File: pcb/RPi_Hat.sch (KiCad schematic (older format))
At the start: 0 parts

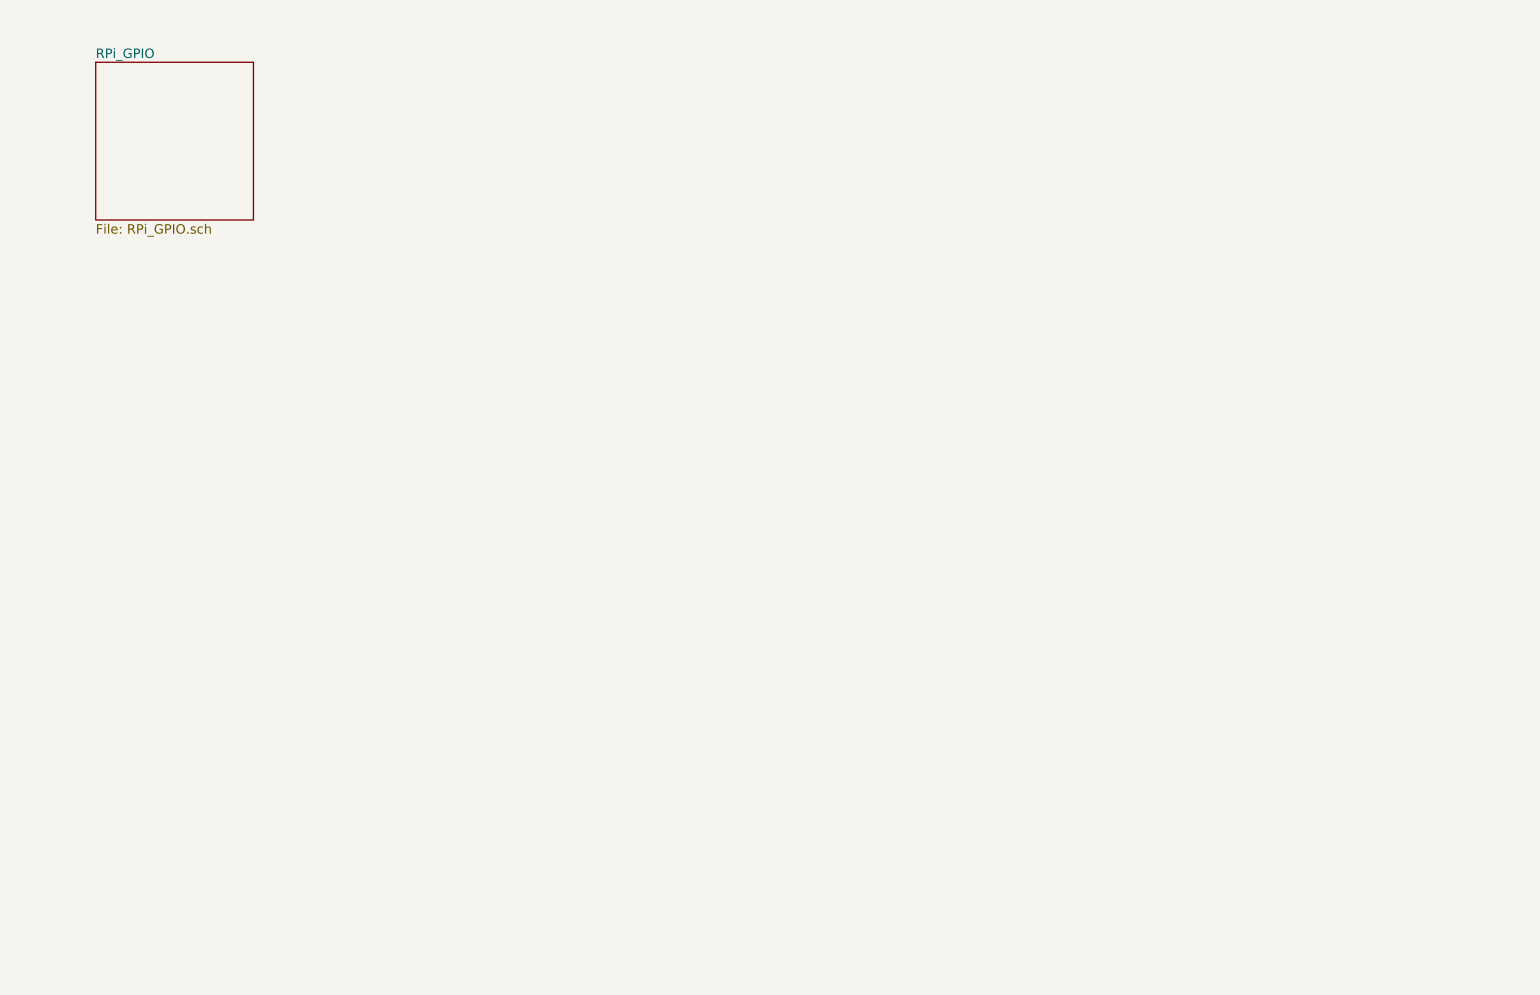
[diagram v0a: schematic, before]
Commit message: Schematic updates
Don't use a relay, use a level shifter so the pin can be used as either
an input or an output.
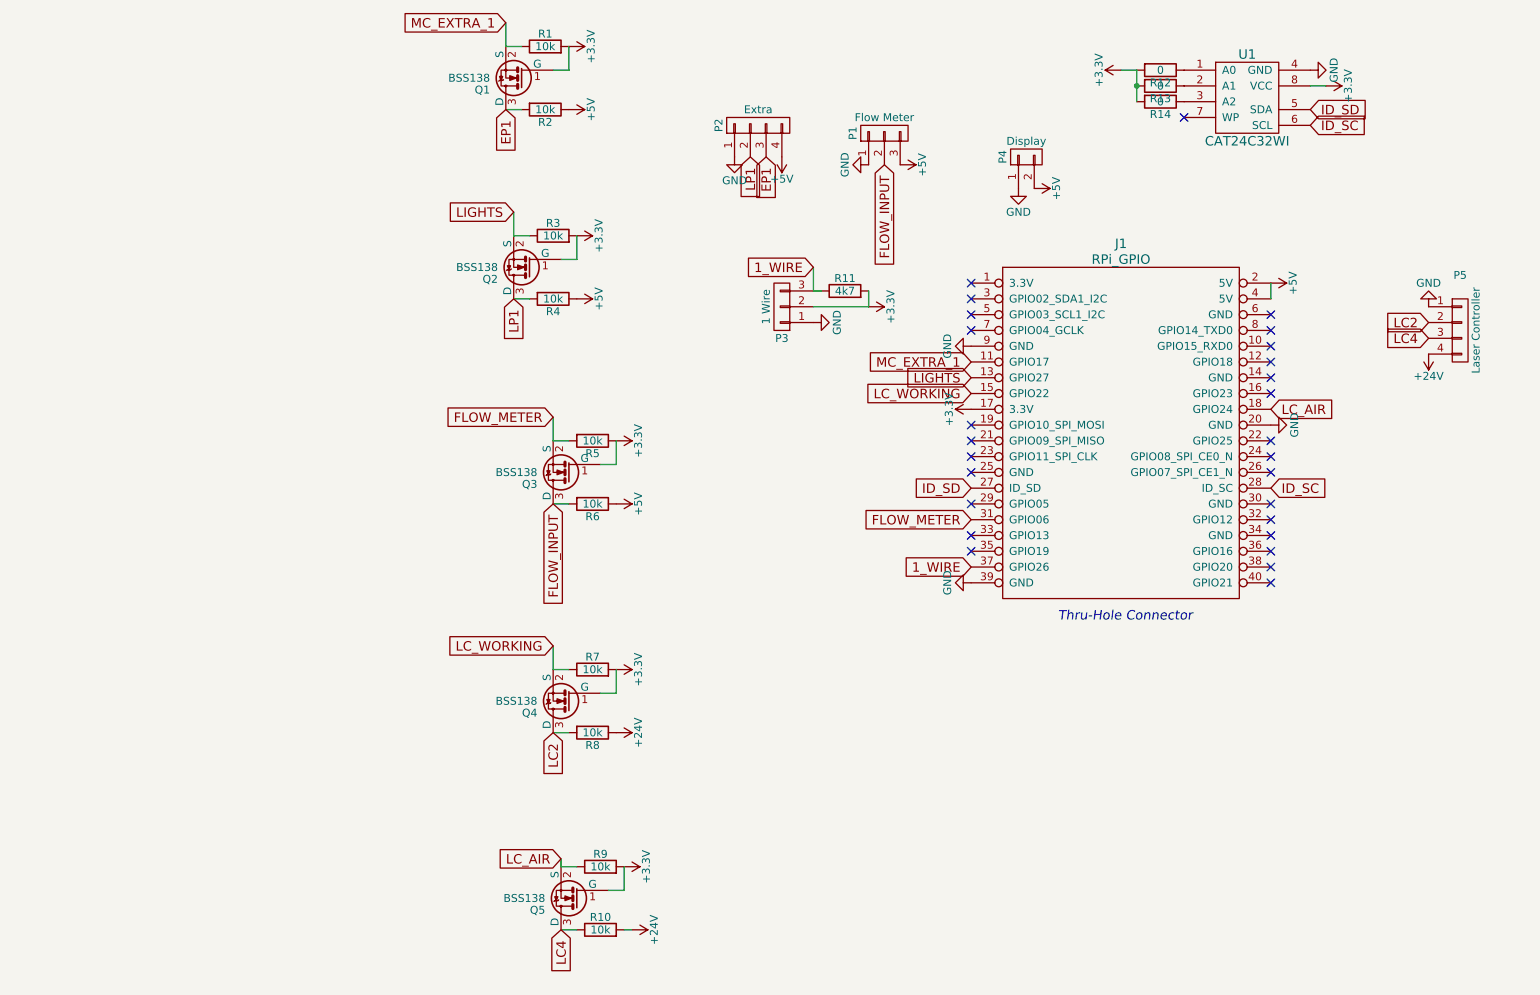
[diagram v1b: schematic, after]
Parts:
- added J1: RPi_GPIO, RPi_Hat:Pin_Header_Straight_2x20, symbol RPi_GPIO
- added P1: Flow Meter, Terminal_Blocks:TerminalBlock_Pheonix_MPT-2.54mm_3pol, symbol CONN_01X03
- added P2: Extra, Terminal_Blocks:TerminalBlock_Pheonix_MPT-2.54mm_5pol, symbol CONN_01X04
- added P3: 1 Wire, Terminal_Blocks:TerminalBlock_Pheonix_MPT-2.54mm_3pol, symbol CONN_01X03
- added P4: Display, Terminal_Blocks:TerminalBlock_Pheonix_MPT-2.54mm_2pol, symbol CONN_01X02
- added P5: Laser Controller, Terminal_Blocks:TerminalBlock_Pheonix_MPT-2.54mm_4pol, symbol CONN_01X04
- added Q1, Q2, Q3, Q4, Q5: BSS138, TO_SOT_Packages_SMD:SOT-23, symbol BSS138
- added R1, R10, R2, R3, R4, R5, R6, R7, R8, R9: 10k, Resistors_SMD:R_1206_HandSoldering, symbol R
- added R11: 4k7, Resistors_SMD:R_1206_HandSoldering, symbol R
- added R12, R13, R14: 0, Resistors_SMD:R_0402, symbol R
- added U1: CAT24C32WI, SMD_Packages:SOIC-8-N, symbol CAT24C32WI
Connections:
- new net: R12.1, U1.1 (A0)
- new net: R13.1, U1.2 (A1)
- new net: R14.1, U1.3 (A2)
- new net +24V: P5.4 (P4), R10.2, R8.1
- new net +3V3: J1.17 (3.3V), P3.2 (P2), Q1.1 (G), Q2.1 (G), Q3.1 (G), Q4.1 (G), Q5.1 (G), R1.2, R11.2, R12.2, R13.2, R14.2, R3.2, R5.1, R7.2, R9.2, U1.8 (VCC)
- new net +5V: J1.2 (5V), J1.4 (5V), P1.3 (P3), P2.4 (P4), P4.2 (P2), R2.1, R4.1, R6.1
- new net 1_WIRE: J1.37 (GPIO26), P3.3 (P3), R11.1
- new net EP1: P2.3 (P3), Q1.3 (D), R2.2
- new net FLOW_INPUT: P1.2 (P2), Q3.3 (D), R6.2
- new net FLOW_METER: J1.31 (GPIO06), Q3.2 (S), R5.2
- new net GND: J1.20 (GND), J1.39 (GND), J1.9 (GND), P1.1 (P1), P2.1 (P1), P3.1 (P1), P4.1 (P1), P5.1 (P1), U1.4 (GND)
- new net ID_SC: J1.28 (ID_SC), U1.6 (SCL)
- new net ID_SD: J1.27 (ID_SD), U1.5 (SDA)
- new net LC2: P5.2 (P2), Q4.3 (D), R8.2
- new net LC4: P5.3 (P3), Q5.3 (D), R10.1
- new net LC_AIR: J1.18 (GPIO24), Q5.2 (S), R9.1
- new net LC_WORKING: J1.15 (GPIO22), Q4.2 (S), R7.1
- new net LIGHTS: J1.13 (GPIO27), Q2.2 (S), R3.1
- new net LP1: P2.2 (P2), Q2.3 (D), R4.2
- new net MC_EXTRA_1: J1.11 (GPIO17), Q1.2 (S), R1.1
- no-connect marks 0 -> 27
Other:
- note added: "Thru-Hole Connector"

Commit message: Add outputs
for the chiller, exhaust, air
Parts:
- added P6: Laser Controller, Terminal_Blocks:TerminalBlock_Pheonix_MPT-2.54mm_4pol, symbol CONN_01X04
- added Q6, Q7, Q8: PZT2222A, TO_SOT_Packages_SMD:SOT-23, symbol PZT2222A
- added R15, R16, R17, R18, R19, R20: 4K7, Resistors_SMD:R_1206_HandSoldering, symbol R
- P2: footprint Terminal_Blocks:TerminalBlock_Pheonix_MPT-2.54mm_5pol -> Terminal_Blocks:TerminalBlock_Pheonix_MPT-2.54mm_4pol
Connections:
- net +5V: now also R18.1, R19.1, R20.1
- net FLOW_METER: now also J1.35 (GPIO19); no longer J1.31 (GPIO06)
- net GND: now also P6.1 (P1), Q6.3 (E), Q7.3 (E), Q8.3 (E)
- net OUT_EXHAUST: now reaches J1.29 (GPIO05)
- net OUT_EXHAUST: now also R15.2
- net OUT_AIR: now reaches J1.33 (GPIO13)
- net OUT_AIR: now also R17.2
- new net: Q7.1 (B), R16.1, R19.2
- new net: Q6.1 (B), R15.1, R18.2
- new net: Q8.1 (B), R17.1, R20.2
- new net HEADER_AIR: P6.2 (P2), Q8.2 (C)
- new net HEADER_CHILLER: P6.3 (P3), Q7.2 (C)
- new net HEADER_EXHAUST: P6.4 (P4), Q6.2 (C)
- new net OUT_CHILLER: J1.31 (GPIO06), R16.2
- no-connect marks 27 -> 24
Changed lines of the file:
@@
 	0    1    1    0
 $EndComp
-Text GLabel 6950 4300 0    60   Input ~ 0
+Text GLabel 6950 4500 0    60   Input ~ 0
 FLOW_METER
 $Comp
@@
 F 0 "P2" H 5600 2050 50  0000 C CNN
 F 1 "Extra" V 5700 1800 50  0000 C CNN
-F 2 "Terminal_Blocks:TerminalBlock_Pheonix_MPT-2.54mm_5pol" V 5800 1750 50  0001 C CNN
+F 2 "Terminal_Blocks:TerminalBlock_Pheonix_MPT-2.54mm_4pol" V 5800 1750 50  0001 C CNN
 F 3 "" H 5600 1800 50  0000 C CNN
 	1    5600 1800
@@
 NoConn ~ 6950 3800
 NoConn ~ 6950 3900
-NoConn ~ 6950 4200
-NoConn ~ 6950 4400
-NoConn ~ 6950 4500
 NoConn ~ 8300 1750
 NoConn ~ 6950 4000
@@
 Text GLabel 4300 4200 3    60   Input ~ 0
 FLOW_INPUT
+Text GLabel 6950 4400 0    60   Input ~ 0
+OUT_AIR
+Text GLabel 6950 4300 0    60   Input ~ 0
+OUT_CHILLER
+Text GLabel 6950 4200 0    60   Input ~ 0
+OUT_EXHAUST
+$Comp
+L PZT2222A Q7
+U 1 1 5705A6E9
+P 2200 5600
+F 0 "Q7" H 2400 5675 50  0000 L CNN
+F 1 "PZT2222A" H 2400 5600 50  0000 L CNN
+F 2 "TO_SOT_Packages_SMD:SOT-23" H 2400 5525 50  0001 L CIN
+F 3 "" H 2200 5600 50  0000 L CNN
+	1    2200 5600
+	1    0    0    -1
+$EndComp
+$Comp
+L R R19
+U 1 1 5705C631
+P 2000 5450
+F 0 "R19" V 2080 5450 50  0000 C CNN
+F 1 "4K7" V 2000 5450 50  0000 C CNN
+F 2 "Resistors_SMD:R_1206_HandSoldering" V 1930 5450 50  0001 C CNN
+F 3 "" H 2000 5450 50  0000 C CNN
+	1    2000 5450
+	1    0    0    -1
+$EndComp
+$Comp
+L R R16
+U 1 1 5705D1DF
+P 1850 5600
+F 0 "R16" V 1930 5600 50  0000 C CNN
+F 1 "4K7" V 1850 5600 50  0000 C CNN
+F 2 "Resistors_SMD:R_1206_HandSoldering" V 1780 5600 50  0001 C CNN
+F 3 "" H 1850 5600 50  0000 C CNN
+	1    1850 5600
+	0    1    1    0
+$EndComp
+$Comp
+L GND #PWR029
+U 1 1 5705D7B5
+P 2300 5800
+F 0 "#PWR029" H 2300 5550 50  0001 C CNN
+F 1 "GND" H 2300 5650 50  0000 C CNN
+F 2 "" H 2300 5800 50  0000 C CNN
+F 3 "" H 2300 5800 50  0000 C CNN
+	1    2300 5800
+	1    0    0    -1
+$EndComp
+$Comp
+L +5V #PWR030
+U 1 1 5705DC40
+P 2000 5300
+F 0 "#PWR030" H 2000 5150 50  0001 C CNN
+F 1 "+5V" H 2000 5440 50  0000 C CNN
+F 2 "" H 2000 5300 50  0000 C CNN
+F 3 "" H 2000 5300 50  0000 C CNN
+	1    2000 5300
+	1    0    0    -1
+$EndComp
+Text GLabel 2300 5400 2    60   Input ~ 0
+HEADER_CHILLER
+$Comp
+L PZT2222A Q6
+U 1 1 5705EC78
+P 2200 4650
+F 0 "Q6" H 2400 4725 50  0000 L CNN
+F 1 "PZT2222A" H 2400 4650 50  0000 L CNN
+F 2 "TO_SOT_Packages_SMD:SOT-23" H 2400 4575 50  0001 L CIN
+F 3 "" H 2200 4650 50  0000 L CNN
+	1    2200 4650
+	1    0    0    -1
+$EndComp
+$Comp
+L R R18
+U 1 1 5705EC7E
+P 2000 4500
+F 0 "R18" V 2080 4500 50  0000 C CNN
+F 1 "4K7" V 2000 4500 50  0000 C CNN
+F 2 "Resistors_SMD:R_1206_HandSoldering" V 1930 4500 50  0001 C CNN
+F 3 "" H 2000 4500 50  0000 C CNN
+	1    2000 4500
+	1    0    0    -1
+$EndComp
+$Comp
+L R R15
+U 1 1 5705EC84
+P 1850 4650
+F 0 "R15" V 1930 4650 50  0000 C CNN
+F 1 "4K7" V 1850 4650 50  0000 C CNN
+F 2 "Resistors_SMD:R_1206_HandSoldering" V 1780 4650 50  0001 C CNN
+F 3 "" H 1850 4650 50  0000 C CNN
+	1    1850 4650
+	0    1    1    0
+$EndComp
+$Comp
+L GND #PWR031
+U 1 1 5705EC8A
+P 2300 4850
+F 0 "#PWR031" H 2300 4600 50  0001 C CNN
+F 1 "GND" H 2300 4700 50  0000 C CNN
+F 2 "" H 2300 4850 50  0000 C CNN
+F 3 "" H 2300 4850 50  0000 C CNN
+	1    2300 4850
+	1    0    0    -1
+$EndComp
+$Comp
+L +5V #PWR032
+U 1 1 5705EC90
+P 2000 4350
+F 0 "#PWR032" H 2000 4200 50  0001 C CNN
+F 1 "+5V" H 2000 4490 50  0000 C CNN
+F 2 "" H 2000 4350 50  0000 C CNN
+F 3 "" H 2000 4350 50  0000 C CNN
+	1    2000 4350
+	1    0    0    -1
+$EndComp
+Text GLabel 2300 4450 2    60   Input ~ 0
+HEADER_EXHAUST
+$Comp
+L PZT2222A Q8
+U 1 1 5705F33E
+P 2200 6550
+F 0 "Q8" H 2400 6625 50  0000 L CNN
+F 1 "PZT2222A" H 2400 6550 50  0000 L CNN
+F 2 "TO_SOT_Packages_SMD:SOT-23" H 2400 6475 50  0001 L CIN
+F 3 "" H 2200 6550 50  0000 L CNN
+	1    2200 6550
+	1    0    0    -1
+$EndComp
+$Comp
+L R R20
+U 1 1 5705F344
+P 2000 6400
+F 0 "R20" V 2080 6400 50  0000 C CNN
+F 1 "4K7" V 2000 6400 50  0000 C CNN
+F 2 "Resistors_SMD:R_1206_HandSoldering" V 1930 6400 50  0001 C CNN
+F 3 "" H 2000 6400 50  0000 C CNN
+	1    2000 6400
+	1    0    0    -1
+$EndComp
+$Comp
+L R R17
+U 1 1 5705F34A
+P 1850 6550
+F 0 "R17" V 1930 6550 50  0000 C CNN
+F 1 "4K7" V 1850 6550 50  0000 C CNN
+F 2 "Resistors_SMD:R_1206_HandSoldering" V 1780 6550 50  0001 C CNN
+F 3 "" H 1850 6550 50  0000 C CNN
+	1    1850 6550
+	0    1    1    0
+$EndComp
+$Comp
+L GND #PWR033
+U 1 1 5705F350
+P 2300 6750
+F 0 "#PWR033" H 2300 6500 50  0001 C CNN
+F 1 "GND" H 2300 6600 50  0000 C CNN
+F 2 "" H 2300 6750 50  0000 C CNN
+F 3 "" H 2300 6750 50  0000 C CNN
+	1    2300 6750
+	1    0    0    -1
+$EndComp
+$Comp
+L +5V #PWR034
+U 1 1 5705F356
+P 2000 6250
+F 0 "#PWR034" H 2000 6100 50  0001 C CNN
+F 1 "+5V" H 2000 6390 50  0000 C CNN
+F 2 "" H 2000 6250 50  0000 C CNN
+F 3 "" H 2000 6250 50  0000 C CNN
+	1    2000 6250
+	1    0    0    -1
+$EndComp
+Text GLabel 2300 6350 2    60   Input ~ 0
+HEADER_AIR
+Text GLabel 1700 6550 0    60   Input ~ 0
+OUT_AIR
+Text GLabel 1700 4650 0    60   Input ~ 0
+OUT_EXHAUST
+Text GLabel 1700 5600 0    60   Input ~ 0
+OUT_CHILLER
+$Comp
+L CONN_01X04 P6
+U 1 1 5706120C
+P 2550 3850
+F 0 "P6" H 2550 4200 50  0000 C CNN
+F 1 "Laser Controller" V 2650 3850 50  0000 C CNN
+F 2 "Terminal_Blocks:TerminalBlock_Pheonix_MPT-2.54mm_4pol" H 2550 3850 50  0001 C CNN
+F 3 "" H 2550 3850 50  0000 C CNN
+	1    2550 3850
+	0    1    1    0
+$EndComp
+$Comp
+L GND #PWR035
+U 1 1 5706186A
+P 2700 3650
+F 0 "#PWR035" H 2700 3400 50  0001 C CNN
+F 1 "GND" H 2700 3500 50  0000 C CNN
+F 2 "" H 2700 3650 50  0000 C CNN
+F 3 "" H 2700 3650 50  0000 C CNN
+	1    2700 3650
+	0    -1   -1   0
+$EndComp
+Text GLabel 2600 3650 1    60   Input ~ 0
+HEADER_AIR
+Text GLabel 2400 3650 1    60   Input ~ 0
+HEADER_EXHAUST
+Text GLabel 2500 3650 1    60   Input ~ 0
+HEADER_CHILLER
 $EndSCHEMATC

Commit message: Add passives for the EEPROM
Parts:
- added C1: 100NF, Capacitors_SMD:C_1206_HandSoldering, symbol CP1_Small
- added JP1: Jumper_NO_Small, Connect:PINHEAD1-2, symbol Jumper_NO_Small
- added R21: 1K, Resistors_SMD:R_1206_HandSoldering, symbol R
- added R22, R23: 3.9K, Resistors_SMD:R_1206_HandSoldering, symbol R
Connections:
- net +3V3: now also C1.2, R21.1, R22.1, R23.1
- net GND: now also C1.1, JP1.1
- net ID_SC: now also R23.2
- net ID_SD: now also R22.2
- net at U1.7 (WP): now also JP1.2, R21.2
- no-connect marks 24 -> 23
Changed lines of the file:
@@
 L +3.3V #PWR020
 U 1 1 570414A5
-P 9200 1550
-F 0 "#PWR020" H 9200 1400 50  0001 C CNN
-F 1 "+3.3V" H 9200 1690 50  0000 C CNN
-F 2 "" H 9200 1550 50  0000 C CNN
-F 3 "" H 9200 1550 50  0000 C CNN
-	1    9200 1550
+P 9600 1550
+F 0 "#PWR020" H 9600 1400 50  0001 C CNN
+F 1 "+3.3V" H 9600 1690 50  0000 C CNN
+F 2 "" H 9600 1550 50  0000 C CNN
+F 3 "" H 9600 1550 50  0000 C CNN
+	1    9600 1550
 	0    1    1    0
 $EndComp
@@
 Text GLabel 6950 4100 0    60   Input ~ 0
 ID_SD
-Text GLabel 9100 1700 2    60   Input ~ 0
+Text GLabel 9700 1700 2    60   Input ~ 0
 ID_SD
-Text GLabel 9100 1800 2    60   Input ~ 0
+Text GLabel 9650 1800 2    60   Input ~ 0
 ID_SC
 Text GLabel 4050 2350 0    60   Input ~ 0
@@
 NoConn ~ 6950 3800
 NoConn ~ 6950 3900
-NoConn ~ 8300 1750
 NoConn ~ 6950 4000
 NoConn ~ 8850 4200
@@
 	8000 1450 7900 1450
 Wire Wire Line
-	9100 1550 9200 1550
+	9100 1550 9600 1550
 Wire Wire Line
 	4000 1700 4100 1700
@@
 Text GLabel 2500 3650 1    60   Input ~ 0
 HEADER_CHILLER
+$Comp
+L CP1_Small C1
+U 1 1 57105950
+P 9500 1450
+F 0 "C1" H 9510 1520 50  0000 L CNN
+F 1 "100NF" V 9650 1400 50  0000 L CNN
+F 2 "Capacitors_SMD:C_1206_HandSoldering" H 9500 1450 50  0001 C CNN
+F 3 "" H 9500 1450 50  0000 C CNN
+	1    9500 1450
+	1    0    0    -1
+$EndComp
+$Comp
+L GND #PWR036
+U 1 1 57105B11
+P 9500 1350
+F 0 "#PWR036" H 9500 1100 50  0001 C CNN
+F 1 "GND" H 9500 1200 50  0000 C CNN
+F 2 "" H 9500 1350 50  0000 C CNN
+F 3 "" H 9500 1350 50  0000 C CNN
+	1    9500 1350
+	-1   0    0    1
+$EndComp
+$Comp
+L R R22
+U 1 1 57105D3C
+P 9250 2000
+F 0 "R22" V 9330 2000 50  0000 C CNN
+F 1 "3.9K" V 9250 2000 50  0000 C CNN
+F 2 "Resistors_SMD:R_1206_HandSoldering" V 9180 2000 50  0001 C CNN
+F 3 "" H 9250 2000 50  0000 C CNN
+	1    9250 2000
+	1    0    0    1
+$EndComp
+$Comp
+L R R23
+U 1 1 57105DDF
+P 9100 2000
+F 0 "R23" V 9180 2000 50  0000 C CNN
+F 1 "3.9K" V 9100 2000 50  0000 C CNN
+F 2 "Resistors_SMD:R_1206_HandSoldering" V 9030 2000 50  0001 C CNN
+F 3 "" H 9100 2000 50  0000 C CNN
+	1    9100 2000
+	-1   0    0    1
+$EndComp
+$Comp
+L +3.3V #PWR037
+U 1 1 5710633A
+P 9400 2150
+F 0 "#PWR037" H 9400 2000 50  0001 C CNN
+F 1 "+3.3V" H 9400 2290 50  0000 C CNN
+F 2 "" H 9400 2150 50  0000 C CNN
+F 3 "" H 9400 2150 50  0000 C CNN
+	1    9400 2150
+	-1   0    0    1
+$EndComp
+$Comp
+L R R21
+U 1 1 571067F6
+P 8300 1900
+F 0 "R21" V 8380 1900 50  0000 C CNN
+F 1 "1K" V 8300 1900 50  0000 C CNN
+F 2 "Resistors_SMD:R_1206_HandSoldering" V 8230 1900 50  0001 C CNN
+F 3 "" H 8300 1900 50  0000 C CNN
+	1    8300 1900
+	-1   0    0    1
+$EndComp
+$Comp
+L +3.3V #PWR038
+U 1 1 57106A2D
+P 8300 2050
+F 0 "#PWR038" H 8300 1900 50  0001 C CNN
+F 1 "+3.3V" H 8300 2190 50  0000 C CNN
+F 2 "" H 8300 2050 50  0000 C CNN
+F 3 "" H 8300 2050 50  0000 C CNN
+	1    8300 2050
+	-1   0    0    1
+$EndComp
+$Comp
+L GND #PWR039
+U 1 1 57106AB0
+P 7750 1750
+F 0 "#PWR039" H 7750 1500 50  0001 C CNN
+F 1 "GND" H 7750 1600 50  0000 C CNN
+F 2 "" H 7750 1750 50  0000 C CNN
+F 3 "" H 7750 1750 50  0000 C CNN
+	1    7750 1750
+	0    1    1    0
+$EndComp
+$Comp
+L Jumper_NO_Small JP1
+U 1 1 57106BD4
+P 7850 1750
+F 0 "JP1" H 7850 1830 50  0000 C CNN
+F 1 "Jumper_NO_Small" H 7860 1690 50  0001 C CNN
+F 2 "Connect:PINHEAD1-2" H 7850 1750 50  0001 C CNN
+F 3 "" H 7850 1750 50  0000 C CNN
+	1    7850 1750
+	1    0    0    -1
+$EndComp
+Wire Wire Line
+	8300 1750 7950 1750
+Connection ~ 9500 1550
+Wire Wire Line
+	9100 1800 9100 1850
+Wire Wire Line
+	9100 2150 9400 2150
+Connection ~ 9250 2150
+Wire Wire Line
+	9100 1800 9650 1800
+Wire Wire Line
+	9100 1700 9700 1700
+Wire Wire Line
+	9250 1850 9250 1700
+Connection ~ 9250 1700
 $EndSCHEMATC

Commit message: Update the schematic
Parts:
- removed Q3: BSS138, TO_SOT_Packages_SMD:SOT-23, symbol BSS138
- removed R5, R6: 10k, Resistors_SMD:R_1206_HandSoldering, symbol R
- added JP2: Relay Voltage Selector, Connect:PINHEAD1-3, symbol JUMPER3
- P5: value Laser Controller -> Laser Controller Input
- P6: value Laser Controller -> Chiller/Air/Exhaust
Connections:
- net FLOW_INPUT is gone; now on net FLOW_METER: P1.2 (P2)
- net +24V: now also JP2.1
- net +3V3: now also P1.3 (P3)
- net +5V: now also JP2.3; no longer P1.3 (P3), R18.1, R19.1, R20.1
- new net VSS: JP2.2, R18.1, R19.1, R20.1
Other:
- note added: "Write Protect"
- moved on the sheet: P4, Q4, R7, R8
